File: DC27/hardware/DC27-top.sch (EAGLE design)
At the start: 32 parts

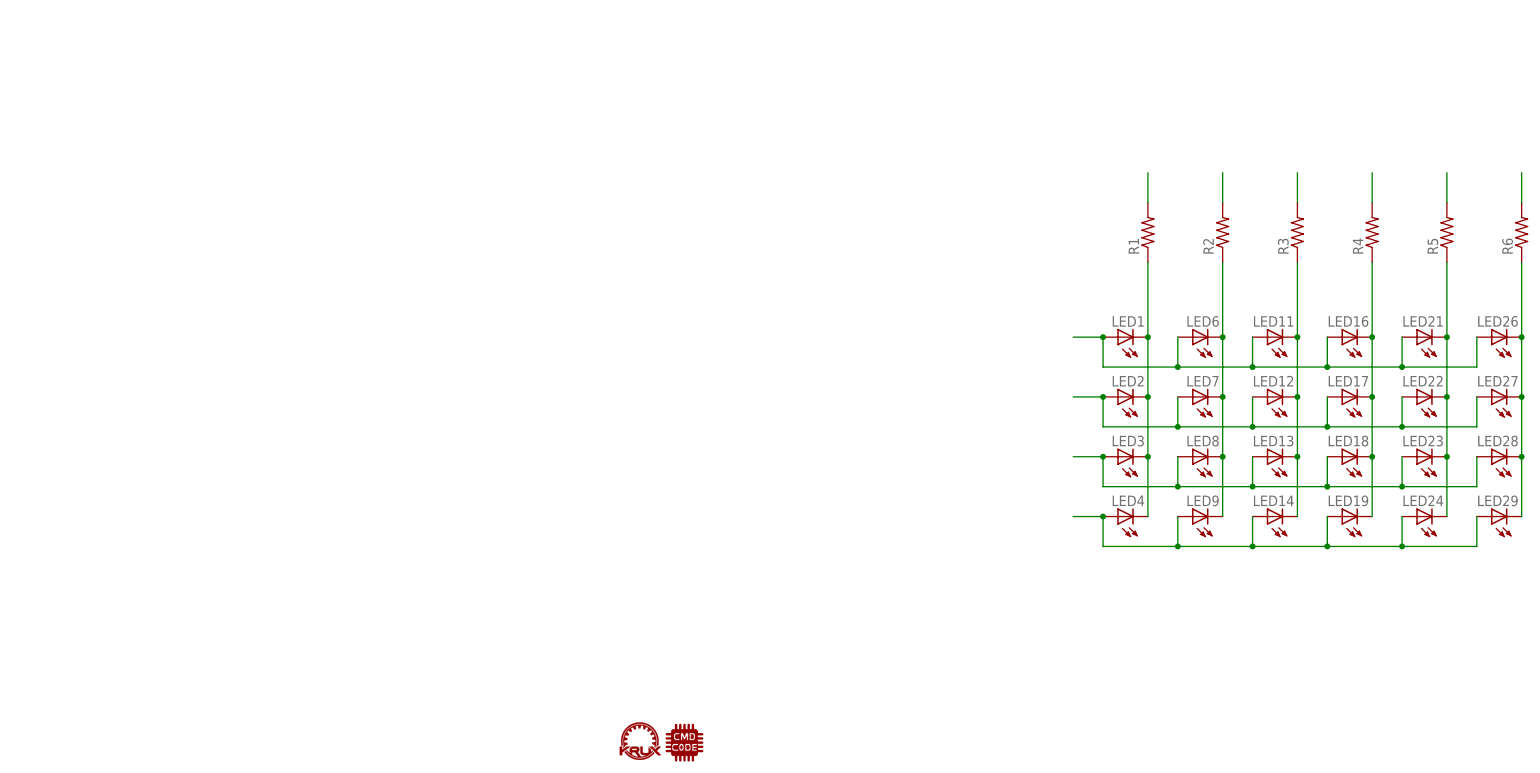
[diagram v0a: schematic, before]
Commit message: started on changes to not charlie plex the leds
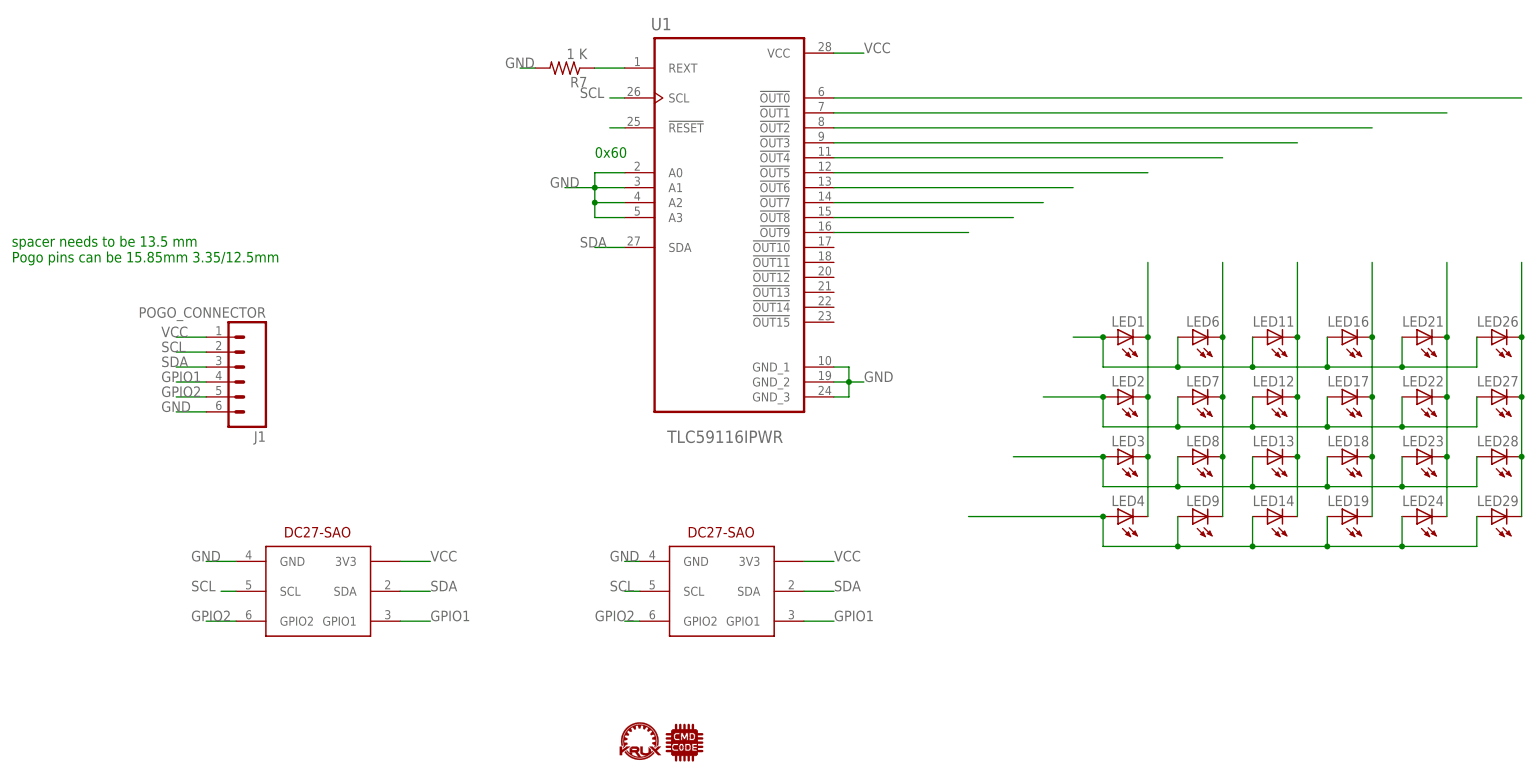
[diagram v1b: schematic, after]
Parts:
- removed R1, R2, R3, R4, R5, R6: (no value), darknet_parts_library:R-US_R0805
- added J1: POGO_CONNECTOR, connector:M06SMD_MALE
- added R7: 1 K, darknet_parts_library:R-US_R0805
- added U$3, U$4: DC-27-SAO, defcon:DC-27-SAO
- added U1: TLC59116IPWR, leds:TLC59116IPWR
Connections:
- new net GND: J1.6, R7.2, U$3.GND, U$4.GND, U1.A0, U1.A1, U1.A2, U1.A3, U1.GND_1, U1.GND_2, U1.GND_3
- new net GPIO1: J1.4, U$3.GPIO1, U$4.GPIO1
- new net GPIO2: J1.5, U$3.GPIO2, U$4.GPIO2
- new net N$10: U1.!OUT6
- new net N$18: R7.1, U1.REXT
- new net N$19: U1.!OUT7
- new net N$20: U1.!RESET
- new net N$21: U1.!OUT8
- new net N$22: U1.!OUT9
- new net SCL: J1.2, U$3.SCL, U$4.SCL, U1.SCL
- new net SDA: J1.3, U$3.SDA, U$4.SDA, U1.SDA
- new net VCC: J1.1, U$3.3V3, U$4.3V3, U1.VCC
- net N$11: no longer R6.1
- net N$12: now also U1.!OUT5; no longer R1.2
- net N$13: now also U1.!OUT4; no longer R2.2
- net N$14: now also U1.!OUT3; no longer R3.2
- net N$15: now also U1.!OUT2; no longer R4.2
- net N$16: now also U1.!OUT1; no longer R5.2
- net N$17: now also U1.!OUT0; no longer R6.2
- net N$5: no longer R1.1
- net N$6: no longer R2.1
- net N$7: no longer R3.1
- net N$8: no longer R4.1
- net N$9: no longer R5.1
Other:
- note added: "0x60"
- note added: "spacer needs to be 13.5 mm Pogo pins can be 15.85mm 3.35/12.5mm"
